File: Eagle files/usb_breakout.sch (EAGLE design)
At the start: 13 parts

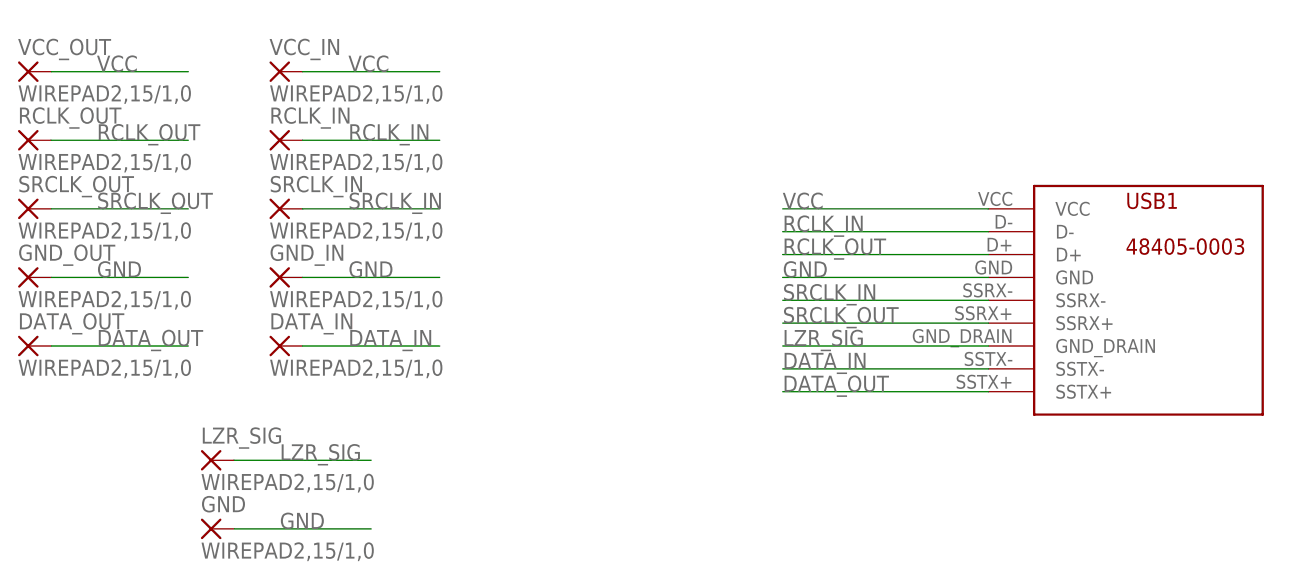
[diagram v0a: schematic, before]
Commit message: Prep for oshpark
Changed naming of BarGraphDriver to be more accurate, added a new bar
graph driver for non-lv boards, fixed the usb breakout to match our
standards and removed the text doc.
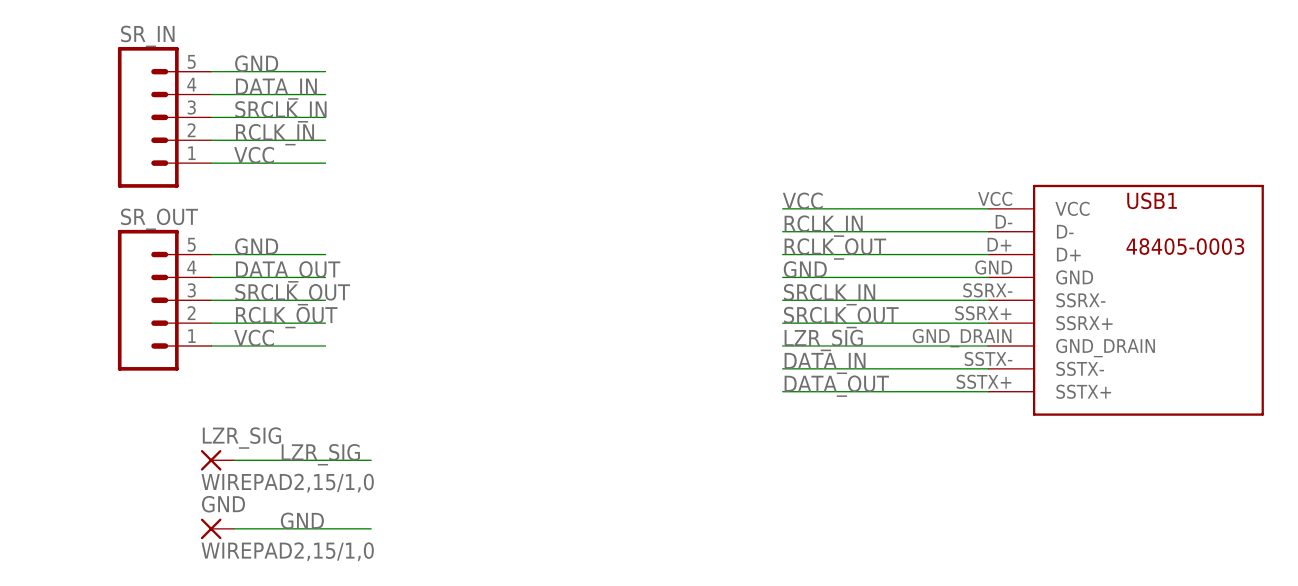
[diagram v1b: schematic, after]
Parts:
- removed DATA_IN, DATA_OUT, GND_IN, GND_OUT, RCLK_IN, RCLK_OUT, SRCLK_IN, SRCLK_OUT: WIREPAD2,15/1,0, wirepad:WIREPAD2,15/1,0
- removed VCC_IN, VCC_OUT: WIREPAD2,15/1,0, smallWirepadSquare:WIREPAD2,15/1,0
- added SR_IN, SR_OUT: (no value), SparkFun-Connectors:M05PTH
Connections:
- net DATA_IN: now also SR_IN.4; no longer DATA_IN.P
- net DATA_OUT: now also SR_OUT.4; no longer DATA_OUT.P
- net GND: now also SR_IN.5, SR_OUT.5; no longer GND_IN.P, GND_OUT.P
- net RCLK_IN: now also SR_IN.2; no longer RCLK_IN.P
- net RCLK_OUT: now also SR_OUT.2; no longer RCLK_OUT.P
- net SRCLK_IN: now also SR_IN.3; no longer SRCLK_IN.P
- net SRCLK_OUT: now also SR_OUT.3; no longer SRCLK_OUT.P
- net VCC: now also SR_IN.1, SR_OUT.1; no longer VCC_IN.P, VCC_OUT.P

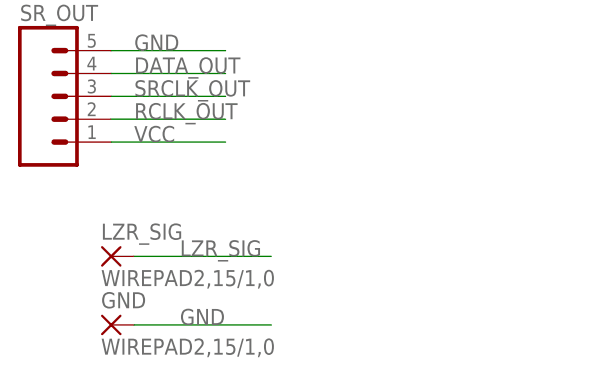
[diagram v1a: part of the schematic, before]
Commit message: aaaaaaaaaaaaaaaaaaaaaaaaaaaaaaaaaaaa
Cleaned up schematics, replaced wire solder points with header pin
mounts for standardization, recreated a broken file and dealt with the
confusion and insanity that followed.
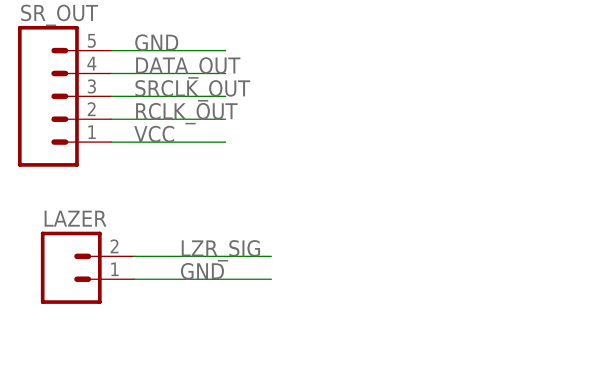
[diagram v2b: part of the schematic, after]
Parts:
- removed GND, LZR_SIG: WIREPAD2,15/1,0, wirepad:WIREPAD2,15/1,0
- added LAZER: (no value), SparkFun-Connectors:M02PTH
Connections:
- net GND: now also LAZER.1; no longer GND.P
- net LZR_SIG: now also LAZER.2; no longer LZR_SIG.P
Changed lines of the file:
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@@
 <parts>
 <part name="USB1" library="my_try" deviceset="48405-0003" device=""/>
-<part name="LZR_SIG" library="wirepad" deviceset="WIREPAD" device="2,15/1,0"/>
-<part name="GND" library="wirepad" deviceset="WIREPAD" device="2,15/1,0"/>
 <part name="SR_IN" library="SparkFun-Connectors" deviceset="M05" device="PTH"/>
 <part name="SR_OUT" library="SparkFun-Connectors" deviceset="M05" device="PTH"/>
+<part name="LAZER" library="SparkFun-Connectors" deviceset="M02" device="PTH"/>
 </parts>
 <sheets>
@@
 <instances>
 <instance part="USB1" gate="G$1" x="68.58" y="40.64"/>
-<instance part="LZR_SIG" gate="G$1" x="-45.72" y="33.02"/>
-<instance part="GND" gate="G$1" x="-45.72" y="25.4"/>
 <instance part="SR_IN" gate="G$1" x="-53.34" y="71.12"/>
 <instance part="SR_OUT" gate="G$1" x="-53.34" y="50.8"/>
+<instance part="LAZER" gate="G$1" x="-50.8" y="30.48"/>
 </instances>
 <busses>
@@
 </segment>
 <segment>
-<pinref part="GND" gate="G$1" pin="P"/>
-<wire x1="-27.94" y1="25.4" x2="-43.18" y2="25.4" width="0.1524" layer="91"/>
-<label x="-38.1" y="25.4" size="1.778" layer="95"/>
+<wire x1="-27.94" y1="30.48" x2="-43.18" y2="30.48" width="0.1524" layer="91"/>
+<label x="-38.1" y="30.48" size="1.778" layer="95"/>
+<pinref part="LAZER" gate="G$1" pin="1"/>
 </segment>
 <segment>
@@
 </segment>
 <segment>
-<pinref part="LZR_SIG" gate="G$1" pin="P"/>
 <wire x1="-27.94" y1="33.02" x2="-43.18" y2="33.02" width="0.1524" layer="91"/>
 <label x="-38.1" y="33.02" size="1.778" layer="95"/>
+<pinref part="LAZER" gate="G$1" pin="2"/>
 </segment>
 </net>
